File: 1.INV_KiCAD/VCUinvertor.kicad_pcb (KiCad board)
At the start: 2 copper layers, 100.7 x 117.9 mm, 118 parts, among them J7 PowerSupply, J9 BRAKE LIGHT, K1 IM06DGR, Q1 2N7002, Q10 2N7002, Q13 BC848C, Q2 2N7002, Q3 2N7002, Q4 2N7002, Q5 2N7002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

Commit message: Small drawing correction
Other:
- board text removed: "Not used"
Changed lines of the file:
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@@
 		(tags "connector wire 0.75sqmm")
 		(property "Reference" "JO27"
-			(at 2.7 -0.05 90)
+			(at 3.8 -0.05 180)
 			(layer "F.SilkS")
 			(effects
@@
 		(tags "connector wire 0.75sqmm")
 		(property "Reference" "JO8"
-			(at 2.9 0 90)
+			(at 3.4 0 180)
 			(layer "F.SilkS")
 			(effects
@@
 		(tags "connector wire 0.75sqmm")
 		(property "Reference" "JO28"
-			(at 0 -2.525 180)
+			(at 3.8 0.05 180)
 			(layer "F.SilkS")
 			(effects
@@
 		(tags "connector wire 0.75sqmm")
 		(property "Reference" "JO7"
-			(at 0.025 2.475 180)
+			(at 3.4 0 180)
 			(layer "F.SilkS")
 			(effects
@@
 		)
 	)
-	(gr_text "Not used"
-		(at 143.22551 90.81774 90)
-		(layer "F.Paste")
-		(effects
-			(font
-				(size 1 1)
-				(thickness 0.15)
-			)
-			(justify left bottom)
-		)
-	)
-	(gr_text "Not used"
-		(at 143.75051 112.66774 90)
-		(layer "F.Paste")
-		(effects
-			(font
-				(size 1 1)
-				(thickness 0.15)
-			)
-			(justify left bottom)
-		)
-	)
 	(gr_text "H_Brk (Yellowish)"
 		(at 134.531348 127.880163 0)
@@
 	)
 	(segment
+		(start 129.30051 60.04274)
+		(end 129.45051 59.89274)
+		(width 0.7)
+		(layer "F.Cu")
+		(net "GND")
+	)
+	(segment
 		(start 119.50051 82.53024)
 		(end 119.41301 82.53024)
@@
 	)
 	(segment
-		(start 129.15051 62.59274)
-		(end 129.30051 62.44274)
-		(width 0.7)
-		(layer "F.Cu")
-		(net "GND")
-	)
-	(segment
 		(start 128.775 151.99325)
 		(end 128.775 151.96774)
@@
 	)
 	(segment
-		(start 129.30051 60.04274)
-		(end 129.45051 59.89274)
-		(width 0.7)
-		(layer "F.Cu")
-		(net "GND")
-	)
-	(segment
 		(start 104.41977 75.704499)
 		(end 103.68426 74.968989)
@@
 	)
 	(segment
+		(start 129.30051 62.44274)
+		(end 129.30051 60.04274)
+		(width 0.7)
+		(layer "F.Cu")
+		(net "GND")
+	)
+	(segment
 		(start 125.40051 104.39274)
 		(end 125.40051 104.14274)
@@
 	)
 	(segment
-		(start 129.30051 62.44274)
-		(end 129.30051 60.04274)
-		(width 0.7)
-		(layer "F.Cu")
-		(net "GND")
-	)
-	(segment
 		(start 124.28801 113.89274)
 		(end 124.43801 113.74274)
@@
 	)
 	(via
-		(at 129.15051 62.59274)
+		(at 129.30051 62.44274)
 		(size 0.6)
 		(drill 0.3)

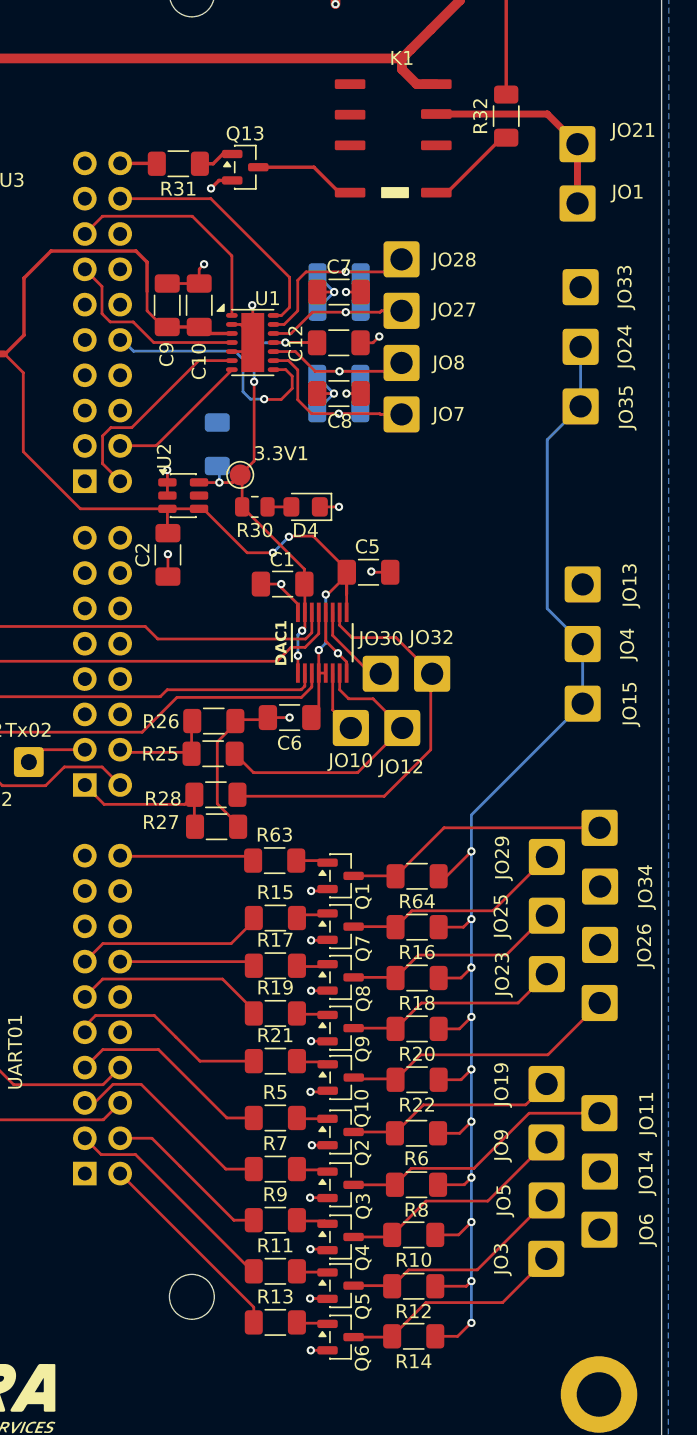
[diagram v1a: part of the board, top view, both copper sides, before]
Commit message: MOS pulldown + missing INV pins added
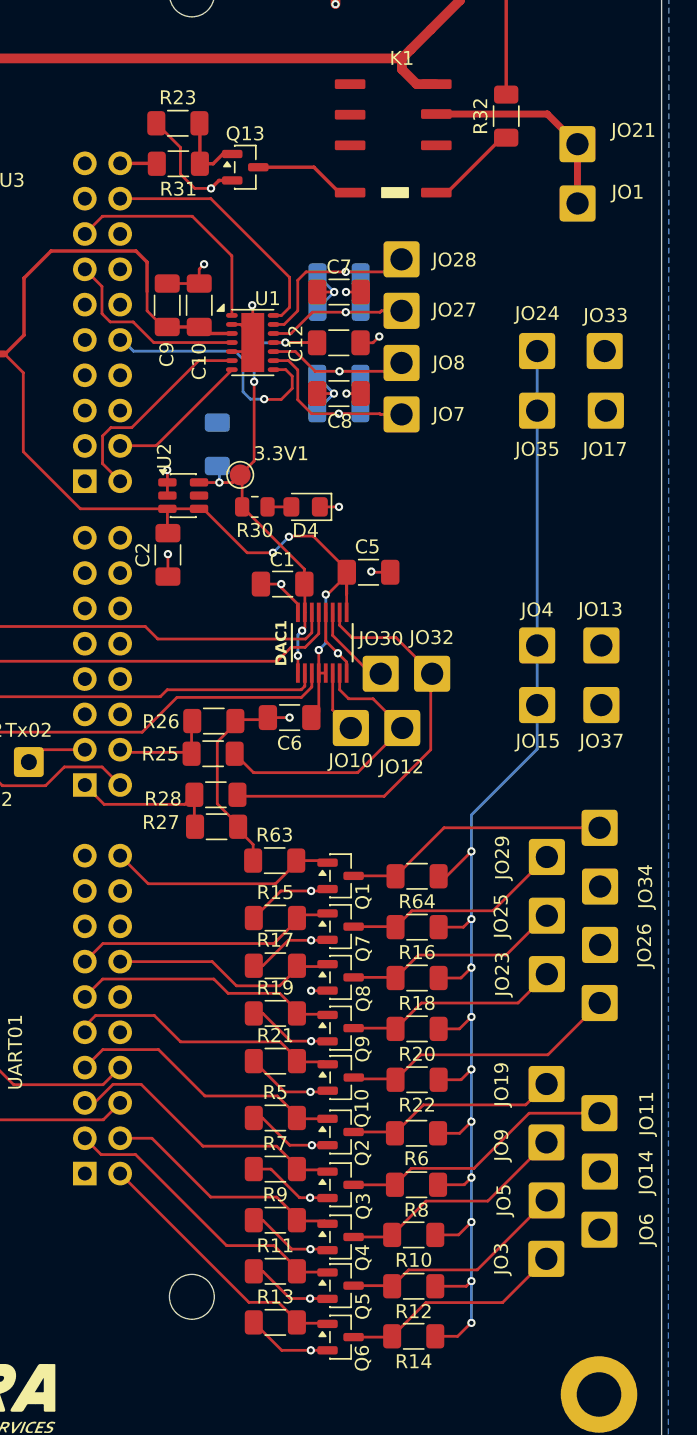
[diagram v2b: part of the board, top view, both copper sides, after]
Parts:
- added JO17: Meter (Dark Gray), Connector_Wire:SolderWire-0.75sqmm_1x01_D1.25mm_OD2.3mm, F.Cu at (148.7, 91.7)
- added JO37: Meter (Dark Gray), Connector_Wire:SolderWire-0.75sqmm_1x01_D1.25mm_OD2.3mm, F.Cu at (148.4, 112.8)
- added R23: 10k, Resistor_SMD:R_1206_3216Metric_Pad1.30x1.75mm_HandSolder, F.Cu at (118.0, 71.0)
- moved JO33 4.91 mm to (148.7, 87.4)
- moved JO13 4.59 mm to (148.4, 108.6)
- moved JO15 3.28 mm to (143.8, 112.8)
- moved JO4 3.28 mm to (143.8, 108.6)
- moved JO35 3.14 mm to (143.8, 91.7)
- moved JO24 3.14 mm to (143.8, 87.4)
- renumbered JO17 to JO38
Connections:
- Q1 pad 1: Net-(Q1-G) -> /NXP_ACC02
- Q10 pad 1: Net-(Q10-G) -> /NXP_REV02
- Q2 pad 1: Net-(Q2-G) -> /NXP_ACC01
- Q3 pad 1: Net-(Q3-G) -> /NXP_ECO01
- Q4 pad 1: Net-(Q4-G) -> /NXP_BRK01
- Q5 pad 1: Net-(Q5-G) -> /NXP_FWD01
- Q6 pad 1: Net-(Q6-G) -> /NXP_REV01
- Q7 pad 1: Net-(Q7-G) -> /NXP_ECO02
- Q8 pad 1: Net-(Q8-G) -> /NXP_BRK02
- Q9 pad 1: Net-(Q9-G) -> /NXP_FWD02
- R11 pad 1: /NXP_FWD01 -> GND
- R11 pad 2: Net-(Q5-G) -> /NXP_FWD01
- R13 pad 1: /NXP_REV01 -> GND
- R13 pad 2: Net-(Q6-G) -> /NXP_REV01
- R15 pad 1: /NXP_ECO02 -> GND
- R15 pad 2: Net-(Q7-G) -> /NXP_ECO02
- R17 pad 1: /NXP_BRK02 -> GND
- R17 pad 2: Net-(Q8-G) -> /NXP_BRK02
- R19 pad 1: /NXP_FWD02 -> GND
- R19 pad 2: Net-(Q9-G) -> /NXP_FWD02
- R21 pad 1: /NXP_REV02 -> GND
- R21 pad 2: Net-(Q10-G) -> /NXP_REV02
- R5 pad 1: /NXP_ACC01 -> GND
- R5 pad 2: Net-(Q2-G) -> /NXP_ACC01
- R63 pad 1: /NXP_ACC02 -> GND
- R63 pad 2: Net-(Q1-G) -> /NXP_ACC02
- R7 pad 1: /NXP_ECO01 -> GND
- R7 pad 2: Net-(Q3-G) -> /NXP_ECO01
- R9 pad 1: /NXP_BRK01 -> GND
- R9 pad 2: Net-(Q4-G) -> /NXP_BRK01
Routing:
- net GND: track 86.3 -> 143.0 mm
- net /NXP_ACC02: track 9.91 -> 16.6 mm
- net /NXP_BRK02: track 9.82 -> 16.4 mm
- net /NXP_REV02: track 14.8 -> 20.3 mm
- net /NXP_BRK01: track 12.2 -> 17.6 mm
- net /NXP_ECO02: track 13.7 -> 19.0 mm
- net /NXP_FWD01: track 16.3 -> 21.6 mm
- net /NXP_FWD02: track 13.9 -> 19.2 mm
- net /NXP_ACC01: track 14.9 -> 20.2 mm
- net /NXP_ECO01: track 15.5 -> 20.7 mm
- net /NXP_REV01: track 14.9 -> 19.5 mm
- net /12V_INV: track 103.4 -> 99.6 mm
- net Net-(Q13-B): track 2.61 -> 5.54 mm
- net Net-(Q7-G): track 2.34 -> 0.00 mm
- net Net-(Q10-G): track 2.34 -> 0.00 mm
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
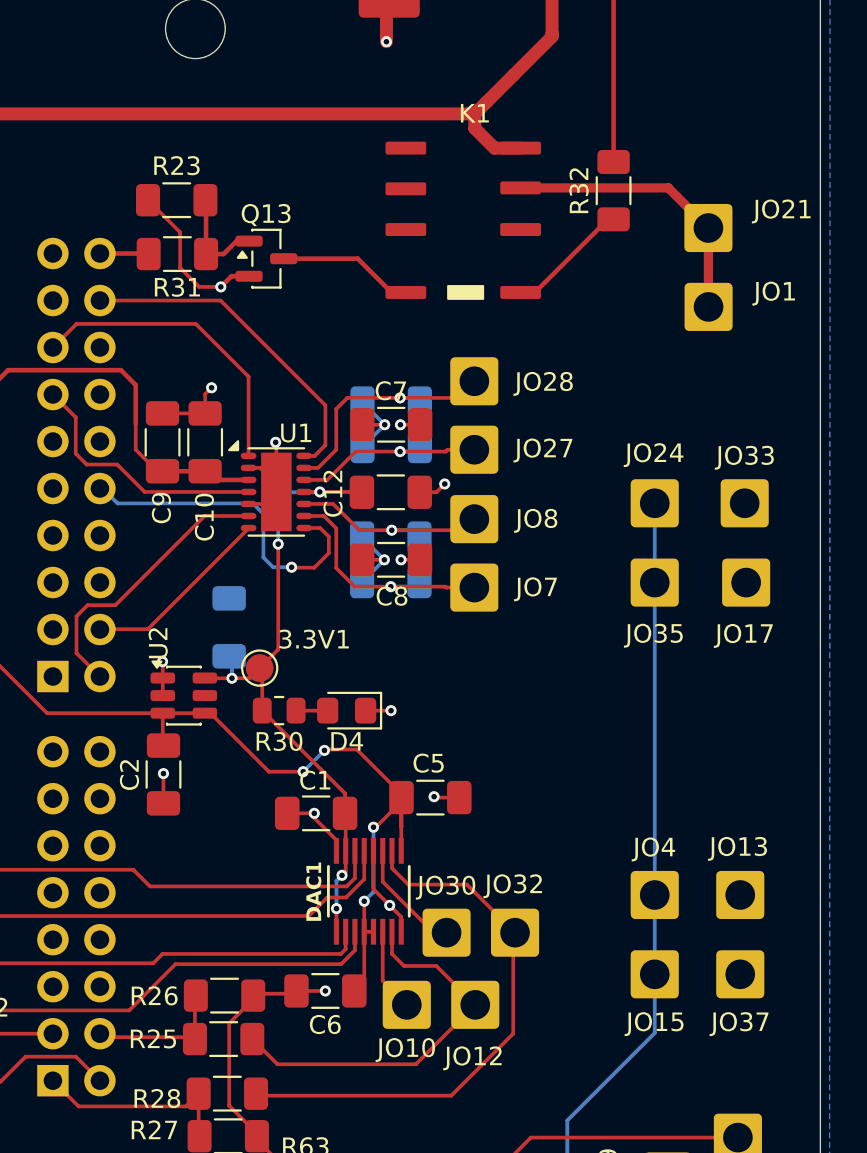
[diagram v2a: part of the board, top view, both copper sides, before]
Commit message: Wire labels correction
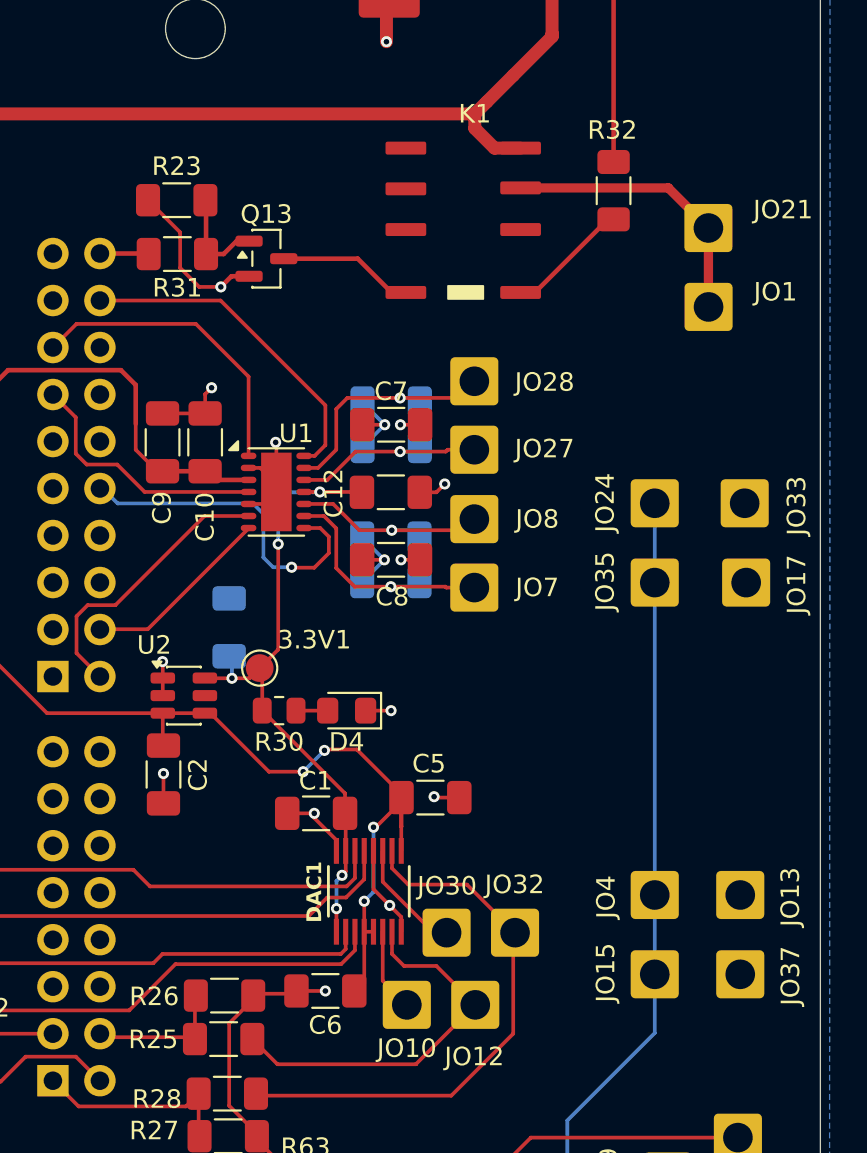
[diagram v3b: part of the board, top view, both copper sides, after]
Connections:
- net /RX0 renamed /RX2
- net /TX0 renamed /TX2
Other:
- board text added: "12V_INV"
- board text added: "Meter (D Gray)"
- board text added: "Not used"

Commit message: Corrections + PUMP&FAN circuit 0.1
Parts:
- C11: moved to F.Cu
- moved 3.3V1 5.54 mm to (126.5, 100.1)
- moved C2 5.33 mm to (122.3, 100.3)
- moved D4 4.06 mm to (131.1, 97.6)
- moved R30 4.06 mm to (127.4, 97.6)
- moved C11 1.92 mm to (122.3, 95.3)
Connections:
- JO1 pad 1: /INV_Supply -> /INV1_VCC
- JO21 pad 1: /INV_Supply -> /INV2_VCC
- K1 pad 3: /INV_Supply -> /INV2_VCC
- K1 pad 5: unconnected-(K1-Pad5) -> BAT+
- K1 pad 6: unconnected-(K1-Pad6) -> /INV1_VCC
- NXP10 pad 1: unconnected-(NXP10-Pin_1-Pad1) -> /RX1
- NXP10 pad 13: /RX1 -> unconnected-(NXP10-Pin_13-Pad13)
- NXP10 pad 15: /TX1 -> unconnected-(NXP10-Pin_15-Pad15)
- NXP10 pad 16: unconnected-(NXP10-Pin_16-Pad16) -> /Pyy
- NXP10 pad 18: /Pyy -> /TX1
- U2 pad 3: +5V -> GND
- U2 pad 5: unconnected-(U2-NR-Pad5) -> GND
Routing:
- net /INV1_VCC: track 0.00 -> 20.6 mm
- net GND: track 143.0 -> 158.8 mm, vias 26 -> 23
- net /INV_Supply: track 15.3 -> 0.00 mm
- net /INV2_VCC: track 0.00 -> 11.0 mm
- net /RX1: track 13.9 -> 23.9 mm
- net +5V: track 105.1 -> 96.3 mm
- net BAT+: track 153.9 -> 145.3 mm
- net +3.3V: track 35.3 -> 36.6 mm, vias 5 -> 4
- net /Pyy: track 18.1 -> 17.1 mm
- net /TX1: track 16.6 -> 15.8 mm

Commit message: PCB Layout with FAN&PUMP MOS - Done
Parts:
- added D10: SS34, Diode_SMD:D_SMA, F.Cu at (100.0, 49.6)
- added D7: SS34, Diode_SMD:D_SMA, F.Cu at (136.7, 49.6)
- added D8: SS34, Diode_SMD:D_SMA, F.Cu at (124.3, 49.6)
- added D9: SS34, Diode_SMD:D_SMA, F.Cu at (112.3, 49.6)
- added J10: FAN2, Connector_JST:JST_PH_B2B-PH-K_1x02_P2.00mm_Vertical, F.Cu at (118.9, 50.7)
- added J11: PUMP1, Connector_JST:JST_PH_B2B-PH-K_1x02_P2.00mm_Vertical, F.Cu at (106.8, 50.7)
- added J12: PUMP2, Connector_JST:JST_PH_B2B-PH-K_1x02_P2.00mm_Vertical, F.Cu at (94.5, 50.7)
- added J8: FAN1, Connector_JST:JST_PH_B2B-PH-K_1x02_P2.00mm_Vertical, F.Cu at (131.2, 50.7)
- added Q11: 2N7002, Package_TO_SOT_SMD:SOT-23, B.Cu at (135.5, 45.4)
- added Q12: 2N7002, Package_TO_SOT_SMD:SOT-23, B.Cu at (123.1, 45.1)
- added Q14: 2N7002, Package_TO_SOT_SMD:SOT-23, B.Cu at (111.0, 45.5)
- added Q15: IRLZ44N, Package_TO_SOT_THT:TO-220-3_Vertical, B.Cu at (136.1, 41.1)
- added Q16: IRLZ44N, Package_TO_SOT_THT:TO-220-3_Vertical, B.Cu at (123.8, 41.1)
- added Q17: IRLZ44N, Package_TO_SOT_THT:TO-220-3_Vertical, B.Cu at (111.7, 41.1)
- added Q18: 2N7002, Package_TO_SOT_SMD:SOT-23, B.Cu at (97.8, 45.6)
- added Q19: IRLZ44N, Package_TO_SOT_THT:TO-220-3_Vertical, B.Cu at (99.4, 41.1)
- added R40: 100k, Resistor_SMD:R_1206_3216Metric_Pad1.30x1.75mm_HandSolder, B.Cu at (136.3, 48.4)
- added R41: 47k, Resistor_SMD:R_1206_3216Metric_Pad1.30x1.75mm_HandSolder, F.Cu at (135.1, 44.3)
- added R42: 100R, Resistor_SMD:R_1206_3216Metric_Pad1.30x1.75mm_HandSolder, B.Cu at (136.3, 50.7)
- added R43: 100R, Resistor_SMD:R_1206_3216Metric_Pad1.30x1.75mm_HandSolder, B.Cu at (124.6, 51.0)
- added R44: 10k, Resistor_SMD:R_1206_3216Metric_Pad1.30x1.75mm_HandSolder, B.Cu at (124.6, 48.7)
- added R45: 47k, Resistor_SMD:R_1206_3216Metric_Pad1.30x1.75mm_HandSolder, F.Cu at (122.7, 44.3)
- added R46: 100R, Resistor_SMD:R_1206_3216Metric_Pad1.30x1.75mm_HandSolder, B.Cu at (111.9, 51.1)
- added R47: 100k, Resistor_SMD:R_1206_3216Metric_Pad1.30x1.75mm_HandSolder, B.Cu at (111.9, 48.8)
- added R48: 47k, Resistor_SMD:R_1206_3216Metric_Pad1.30x1.75mm_HandSolder, F.Cu at (110.7, 44.3)
- added R49: 100R, Resistor_SMD:R_1206_3216Metric_Pad1.30x1.75mm_HandSolder, B.Cu at (99.0, 51.1)
- added R50: 100k, Resistor_SMD:R_1206_3216Metric_Pad1.30x1.75mm_HandSolder, B.Cu at (99.0, 48.8)
- added R51: 47k, Resistor_SMD:R_1206_3216Metric_Pad1.30x1.75mm_HandSolder, F.Cu at (98.4, 44.3)
- added R52: 100R, Resistor_SMD:R_0805_2012Metric, F.Cu at (120.1, 141.4)
- added R53: 100R, Resistor_SMD:R_0805_2012Metric, F.Cu at (119.9, 144.3)
- added R54: 100R, Resistor_SMD:R_0805_2012Metric, F.Cu at (117.5, 146.4)
- added R55: 100R, Resistor_SMD:R_0805_2012Metric, F.Cu at (119.9, 147.7)
- added R56: 100R, Resistor_SMD:R_0805_2012Metric, F.Cu at (117.3, 150.5)
- added R57: 100R, Resistor_SMD:R_0805_2012Metric, F.Cu at (120.1, 138.1)
- added R58: 100R, Resistor_SMD:R_0805_2012Metric, F.Cu at (118.9, 131.9)
- added R59: 100R, Resistor_SMD:R_0805_2012Metric, F.Cu at (118.9, 128.7)
- added R60: 100R, Resistor_SMD:R_0805_2012Metric, F.Cu at (118.9, 125.5)
- added R61: 100R, Resistor_SMD:R_0805_2012Metric, F.Cu at (120.1, 135.0)
- R11, R15, R17, R19, R5, R63, R7, R9: value 10k -> 100k
- moved J9 21.8 mm to (71.9, 54.2)
- moved H1 20.7 mm to (148.3, 32.8)
- moved H2 20.7 mm to (56.5, 32.8)
- moved J7 17.3 mm to (136.9, 62.0), turned to 90 degrees
- moved D2 16.4 mm to (145.5, 60.0), turned to 90 degrees
- moved VCC_BAT1 11.5 mm to (146.0, 51.7), turned to 180 degrees
- moved K1 2.46 mm to (129.7, 70.0)
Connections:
- Q1 pad 1: /NXP_ACC02 -> Net-(Q1-G)
- Q10 pad 1: /NXP_REV02 -> Net-(Q10-G)
- Q2 pad 1: /NXP_ACC01 -> Net-(Q2-G)
- Q3 pad 1: /NXP_ECO01 -> Net-(Q3-G)
- Q4 pad 1: /NXP_BRK01 -> Net-(Q4-G)
- Q5 pad 1: /NXP_FWD01 -> Net-(Q5-G)
- Q6 pad 1: /NXP_REV01 -> Net-(Q6-G)
- Q7 pad 1: /NXP_ECO02 -> Net-(Q7-G)
- Q8 pad 1: /NXP_BRK02 -> Net-(Q8-G)
- Q9 pad 1: /NXP_FWD02 -> Net-(Q9-G)
- R11 pad 2: /NXP_FWD01 -> Net-(Q5-G)
- R13 pad 2: /NXP_REV01 -> Net-(Q6-G)
- R15 pad 2: /NXP_ECO02 -> Net-(Q7-G)
- R17 pad 2: /NXP_BRK02 -> Net-(Q8-G)
- R19 pad 2: /NXP_FWD02 -> Net-(Q9-G)
- R21 pad 2: /NXP_REV02 -> Net-(Q10-G)
- R5 pad 2: /NXP_ACC01 -> Net-(Q2-G)
- R63 pad 2: /NXP_ACC02 -> Net-(Q1-G)
- R7 pad 2: /NXP_ECO01 -> Net-(Q3-G)
- R9 pad 2: /NXP_BRK01 -> Net-(Q4-G)
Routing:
- net BAT+: track 145.3 -> 250.6 mm
- net unconnected-(NXP13-Pin_11-Pad11): track 0.00 -> 69.0 mm
- net unconnected-(NXP13-Pin_9-Pad9): track 0.00 -> 64.6 mm
- net unconnected-(NXP13-Pin_7-Pad7): track 0.00 -> 62.6 mm
- net unconnected-(NXP13-Pin_5-Pad5): track 0.00 -> 61.2 mm
- net GND: track 158.8 -> 193.0 mm
- net BRAKELIGHT: track 47.4 -> 32.7 mm
- net /NXP_REV01: track 19.5 -> 4.77 mm
- net Net-(Q6-G): track 0.00 -> 13.9 mm
- net Net-(D8-A): track 0.00 -> 13.6 mm
- net Net-(D10-A): track 0.00 -> 13.6 mm
- net Net-(D9-A): track 0.00 -> 13.6 mm
- net Net-(D7-A): track 0.00 -> 13.6 mm
- net /NXP_BRK01: track 17.6 -> 4.35 mm
- net Net-(Q4-G): track 0.00 -> 12.5 mm
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- added copper zone on F.Cu, net GND
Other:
- board size 100.7 x 117.9 mm -> 100.7 x 138.5 mm

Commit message: Hole_mounting displacement correction
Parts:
- moved H2 11.6 mm to (56.6, 44.3)
- moved H1 11.6 mm to (148.3, 44.3)
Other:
- board text added: "HEATSINK"
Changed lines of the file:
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@@
 	)
 	(footprint "MountingHole:MountingHole_3.2mm_M3_ISO14580_Pad"
+		(locked yes)
 		(layer "F.Cu")
-		(at 148.294615 32.772116)
+		(at 148.25051 44.34274)
 		(descr "Mounting Hole 3.2mm, M3, generated by kicad-footprint-generator mountinghole.py")
 		(tags "mountinghole M3 ISO14580")
@@
 	)
 	(footprint "MountingHole:MountingHole_3.2mm_M3_ISO14580_Pad"
+		(locked yes)
 		(layer "F.Cu")
-		(at 56.494615 32.772116)
+		(at 56.55051 44.34274)
 		(descr "Mounting Hole 3.2mm, M3, generated by kicad-footprint-generator mountinghole.py")
 		(tags "mountinghole M3 ISO14580")
@@
 			)
 			(justify left bottom mirror)
+		)
+	)
+	(gr_text "HEATSINK"
+		(at 125.45051 34.74274 0)
+		(layer "B.Paste")
+		(effects
+			(font
+				(size 3 3)
+				(thickness 0.4)
+			)
+			(justify left bottom mirror)

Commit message: INV pinout+ layout changes - Done
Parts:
- added R24: 100k, Resistor_SMD:R_1206_3216Metric_Pad1.30x1.75mm_HandSolder, F.Cu at (119.9, 109.3)
- J7: footprint Connector_JST:JST_PH_B2B-PH-K_1x02_P2.00mm_Vertical -> Connector_Phoenix_GMSTB:PhoenixContact_GMSTBVA_2,5_2-G-7,62_1x02_P7.62mm_Vertical
- moved D2 76.2 mm to (70.7, 45.4), turned to 180 degrees
- moved J7 68.0 mm to (74.6, 34.8), turned to 180 degrees
- moved VCC_BAT1 61.2 mm to (84.9, 48.5)
- moved JO2 5.41 mm to (101.9, 116.6)
- moved JO16 1.82 mm to (105.5, 116.6)
- moved JO20 1.82 mm to (98.2, 116.6)
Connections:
- DAC1 pad 9: +3.3V -> /DAC_PD
- NXP10 pad 12: unconnected-(NXP10-Pin_12-Pad12) -> /Pyy
- NXP10 pad 16: /Pyy -> unconnected-(NXP10-Pin_16-Pad16)
- NXP11 pad 1: NXP_TPSOUT02 -> unconnected-(NXP11-Pin_1-Pad1)
- NXP11 pad 2: /Rx_UART02 -> unconnected-(NXP11-Pin_2-Pad2)
- NXP11 pad 3: /Tx_UART02 -> NXP_TPSOUT01
- NXP11 pad 4: NXP_TPSOUT01 -> unconnected-(NXP11-Pin_4-Pad4)
- NXP11 pad 5: unconnected-(NXP11-Pin_5-Pad5) -> NXP_TPSOUT02
- NXP11 pad 8: unconnected-(NXP11-Pin_8-Pad8) -> /DAC_PD
- NXP12 pad 17: unconnected-(NXP12-Pin_17-Pad17) -> /NXP_ACC02
- NXP12 pad 19: unconnected-(NXP12-Pin_19-Pad19) -> /Tx_UART02
- NXP12 pad 20: /NXP_ACC02 -> /Rx_UART02
- NXP13 pad 11: unconnected-(NXP13-Pin_11-Pad11) -> /FAN1
- NXP13 pad 5: unconnected-(NXP13-Pin_5-Pad5) -> /PUMP2
- NXP13 pad 7: unconnected-(NXP13-Pin_7-Pad7) -> /PUMP1
- NXP13 pad 9: unconnected-(NXP13-Pin_9-Pad9) -> /FAN2
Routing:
- net /FAN1: track 0.00 -> 90.3 mm
- net /FAN2: track 0.00 -> 77.5 mm
- net /PUMP2: track 0.00 -> 71.9 mm
- net unconnected-(NXP13-Pin_11-Pad11): track 69.0 -> 0.00 mm
- net /PUMP1: track 0.00 -> 66.8 mm
- net unconnected-(NXP13-Pin_9-Pad9): track 64.6 -> 0.00 mm
- net unconnected-(NXP13-Pin_7-Pad7): track 62.6 -> 0.00 mm
- net unconnected-(NXP13-Pin_5-Pad5): track 61.2 -> 0.00 mm
- net GND: track 193.0 -> 226.4 mm, vias 23 -> 24
- net BAT+: track 250.6 -> 235.8 mm
- net /DAC_PD: track 0.00 -> 13.1 mm
- net NXP_TPSOUT02: track 11.1 -> 19.7 mm
- net /Tx_UART02: track 4.03 -> 12.3 mm
- net +3.3V: track 36.6 -> 32.0 mm, vias 4 -> 2
- net NXP_TPSOUT01: track 7.63 -> 11.2 mm
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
